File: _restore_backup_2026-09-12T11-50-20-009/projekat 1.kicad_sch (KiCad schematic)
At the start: 233 parts, among them J1 Conn_01x02_Pin, J2 Conn_01x02_Pin, J3 Output signal, J4 Conn_01x02_Pin, K1 Relay_SPST-NO_SSB (G6B-1177C(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, K2 Relay_SPST-NO_CW (G6B-1177C(-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, Q1 BC547, Q2 BC547, Q3 BC549, Q4 BC549, Q5 BC549, Q6 BC547, Q7 IRF510, Q9 BC547, SW1 on/off_12V, SW3 audio_SsbMorse_selektor, SW4 on/off_zujanje, SW5 keying_CW_SSB_selektor, SW6 selektor_modulacija, SW7 selektor_izlaza, U1 LM386, U10 OPA656UB, U11 L7806, U12 LM386, U13 OPA656UB, U14 OPA656UB, U15 OPA656UB, U2 LM358, U3 LM358, U4 LM358, U5 OPA656UB, U6 4N35, U7 OPA656UB, U8 OPA656UB, U9 OPA656UB

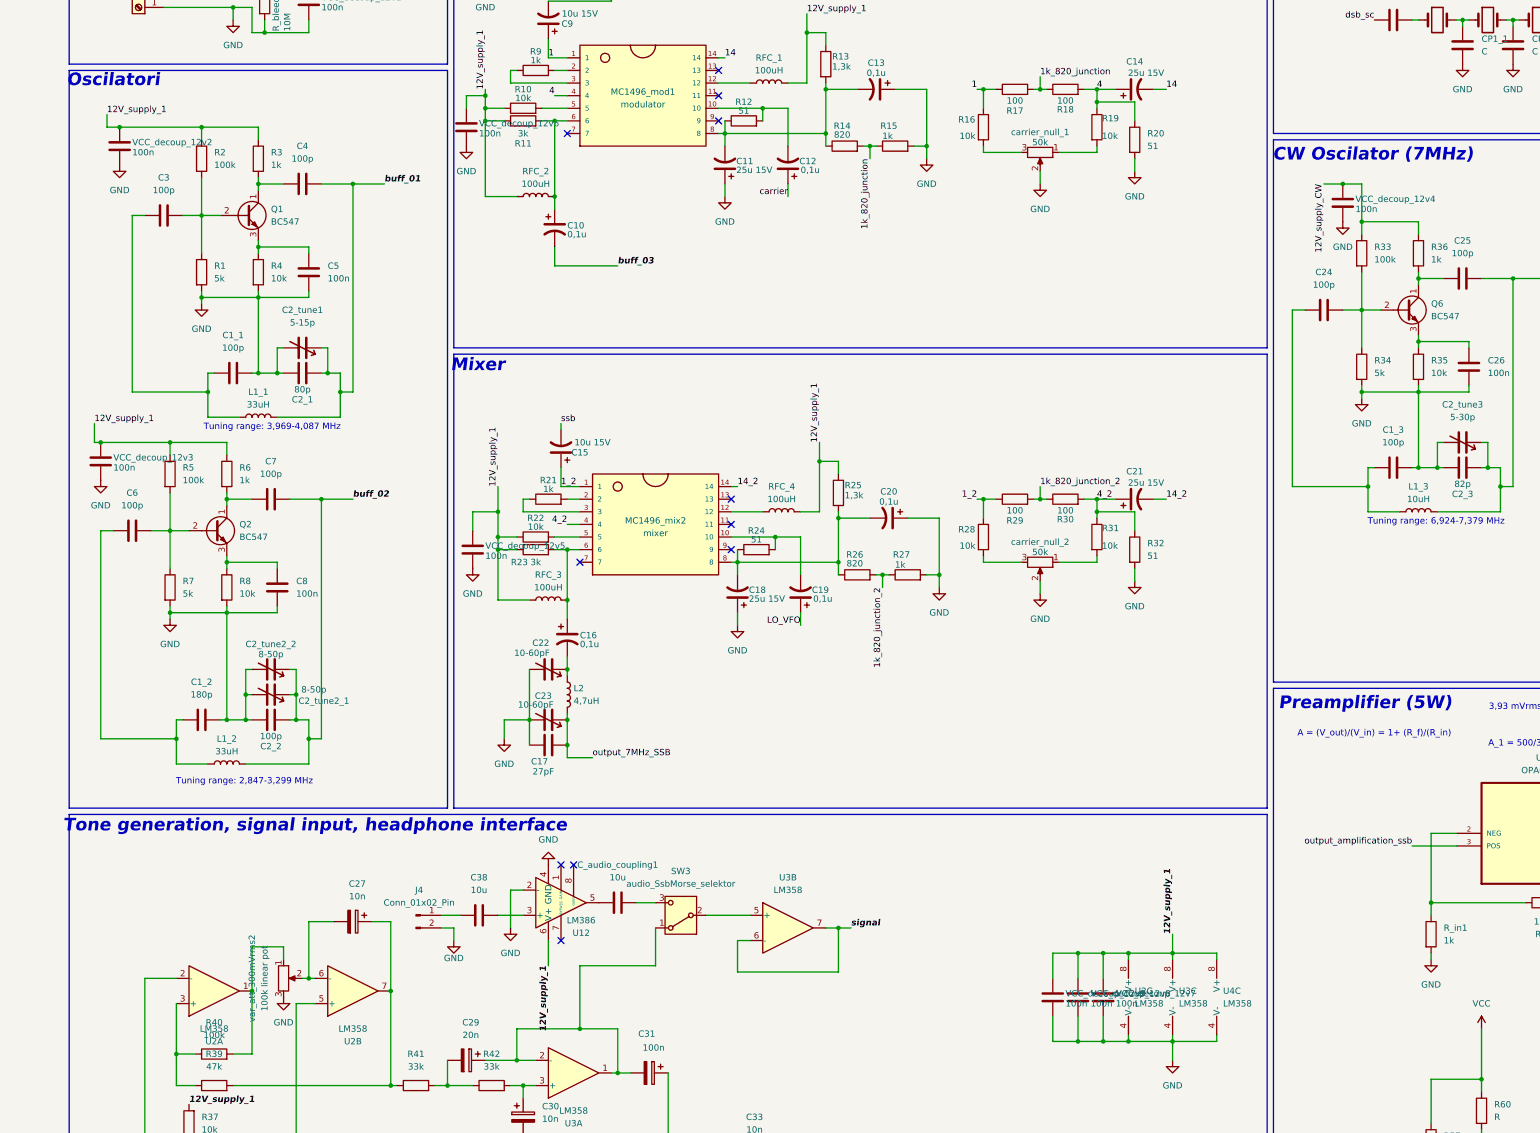
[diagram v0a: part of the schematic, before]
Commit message: Dodati decoupling koncdnzatori na sve blokove i operacione, obrisan gornji layer bakra, sve vije prebačene na through, drc zadaje erore da su netovi šortivani
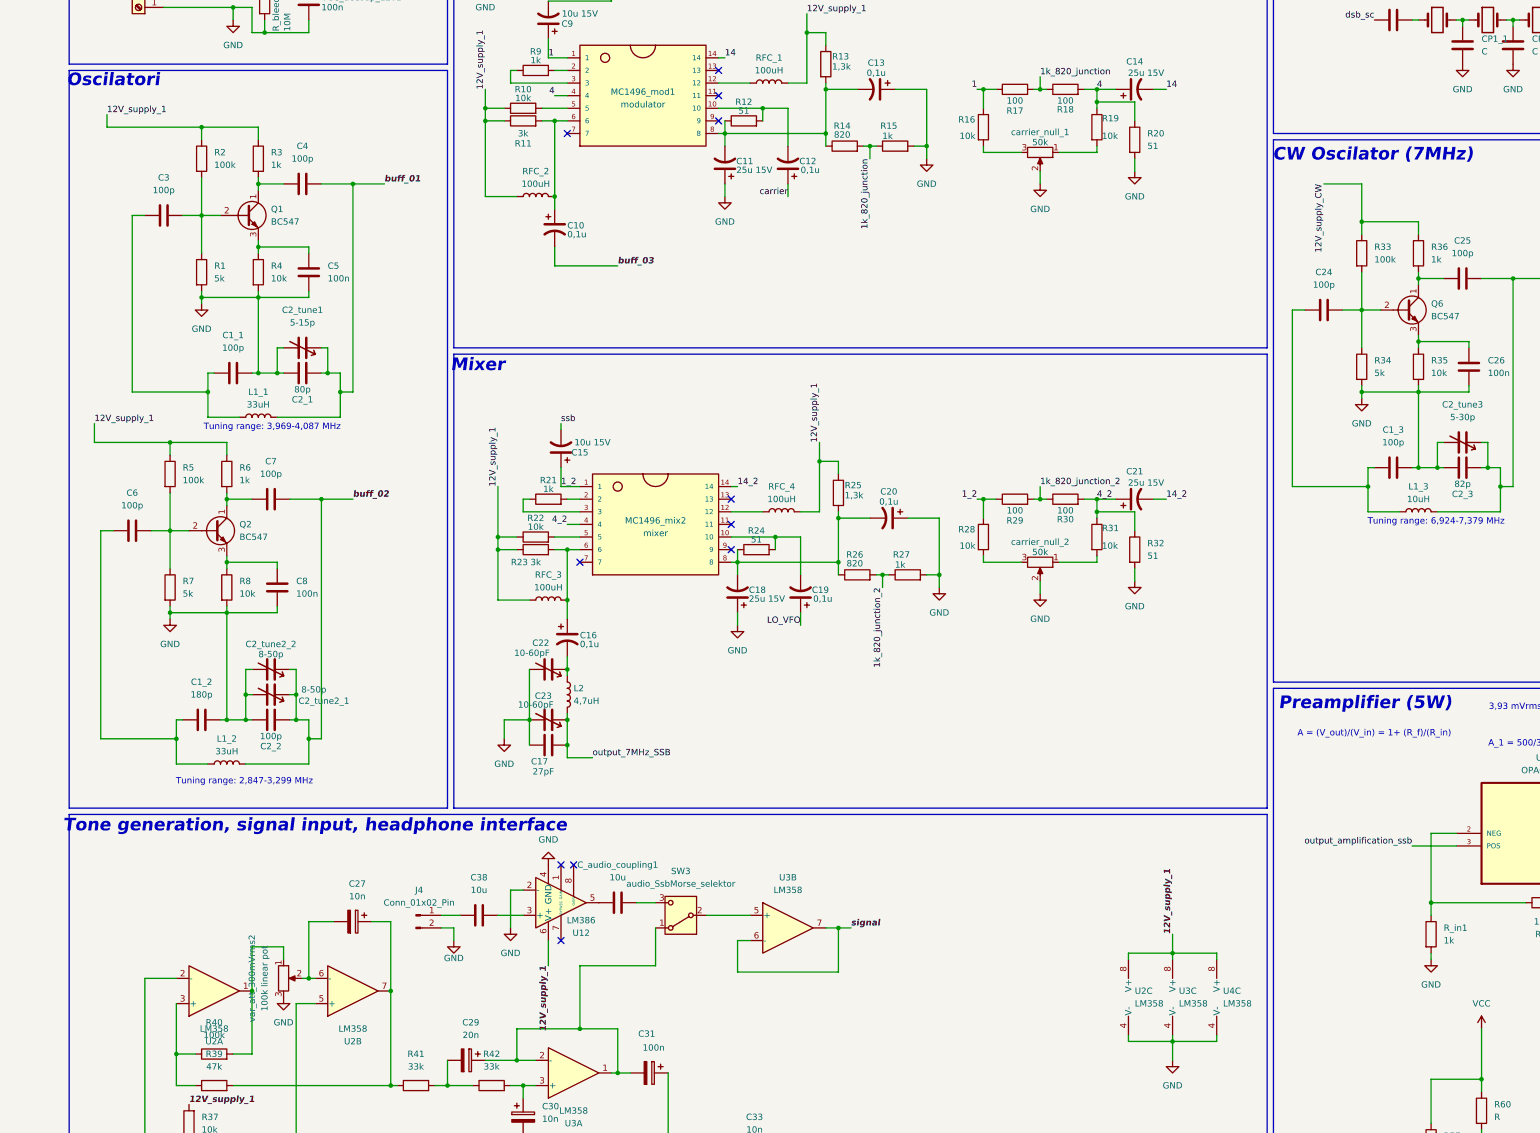
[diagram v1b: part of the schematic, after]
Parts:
- removed VCC_decoup_12v2, VCC_decoup_12v3, VCC_decoup_12v4, VCC_decoup_12v5, VCC_decoup_12v6, VCC_decoup_12v7, VCC_decoup_12v8, VCC_decoup_12v9: 100n, Capacitor_SMD:C_1206_3216Metric, symbol Device:C
